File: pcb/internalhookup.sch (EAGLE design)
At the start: 8 parts, among them CN1 LASER, J2 SERVO, J5 CONTROL, Q1 600mA/40V, U1 AMS1117-3.3

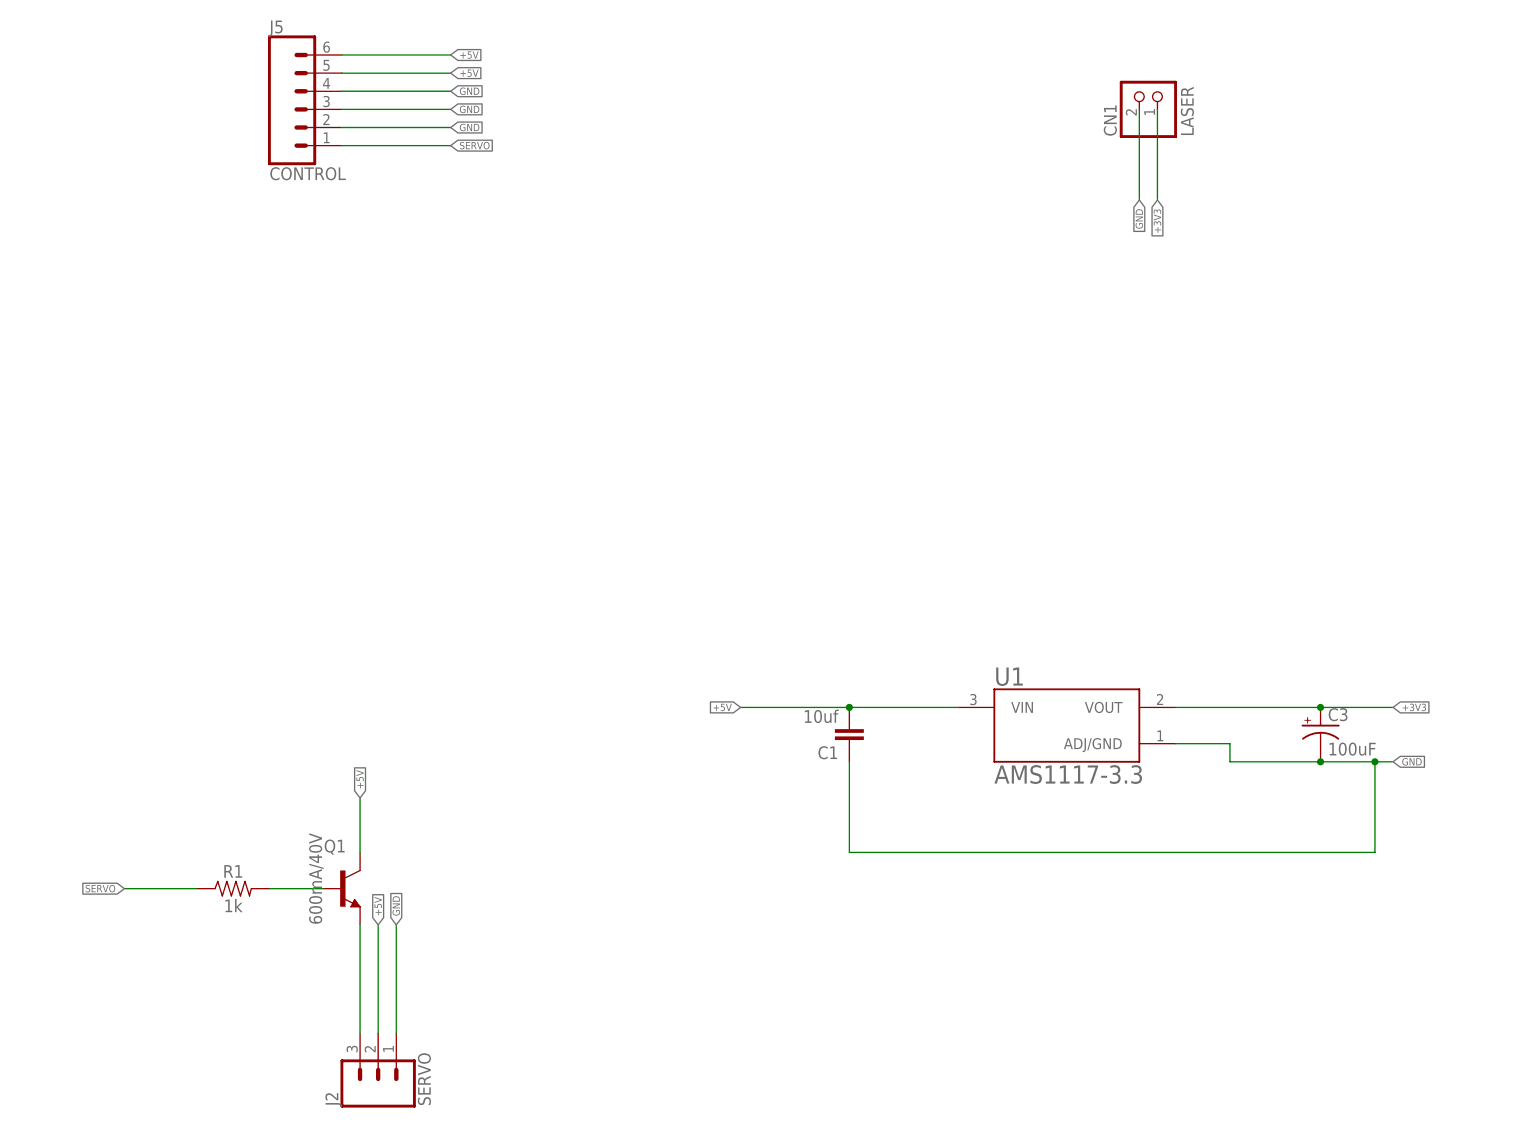
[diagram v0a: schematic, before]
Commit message: Updating to the latest PCB to fix breaking issues
* Fixed capacitor sets for both boards to be larger and polarized on the
LDO's
* Fixed left track for motor board as it was 1 pin too short
* Switched from Declination to Azimuth
* Moved Azimuth signaling to the internal board to allow for movement
* Removed resistors on 5V LED signal buffer
* Switch LED pinout to match the Lumenati ordering
* Internal board got a polarized capacitor
* Internal board layout moved around to better match reality
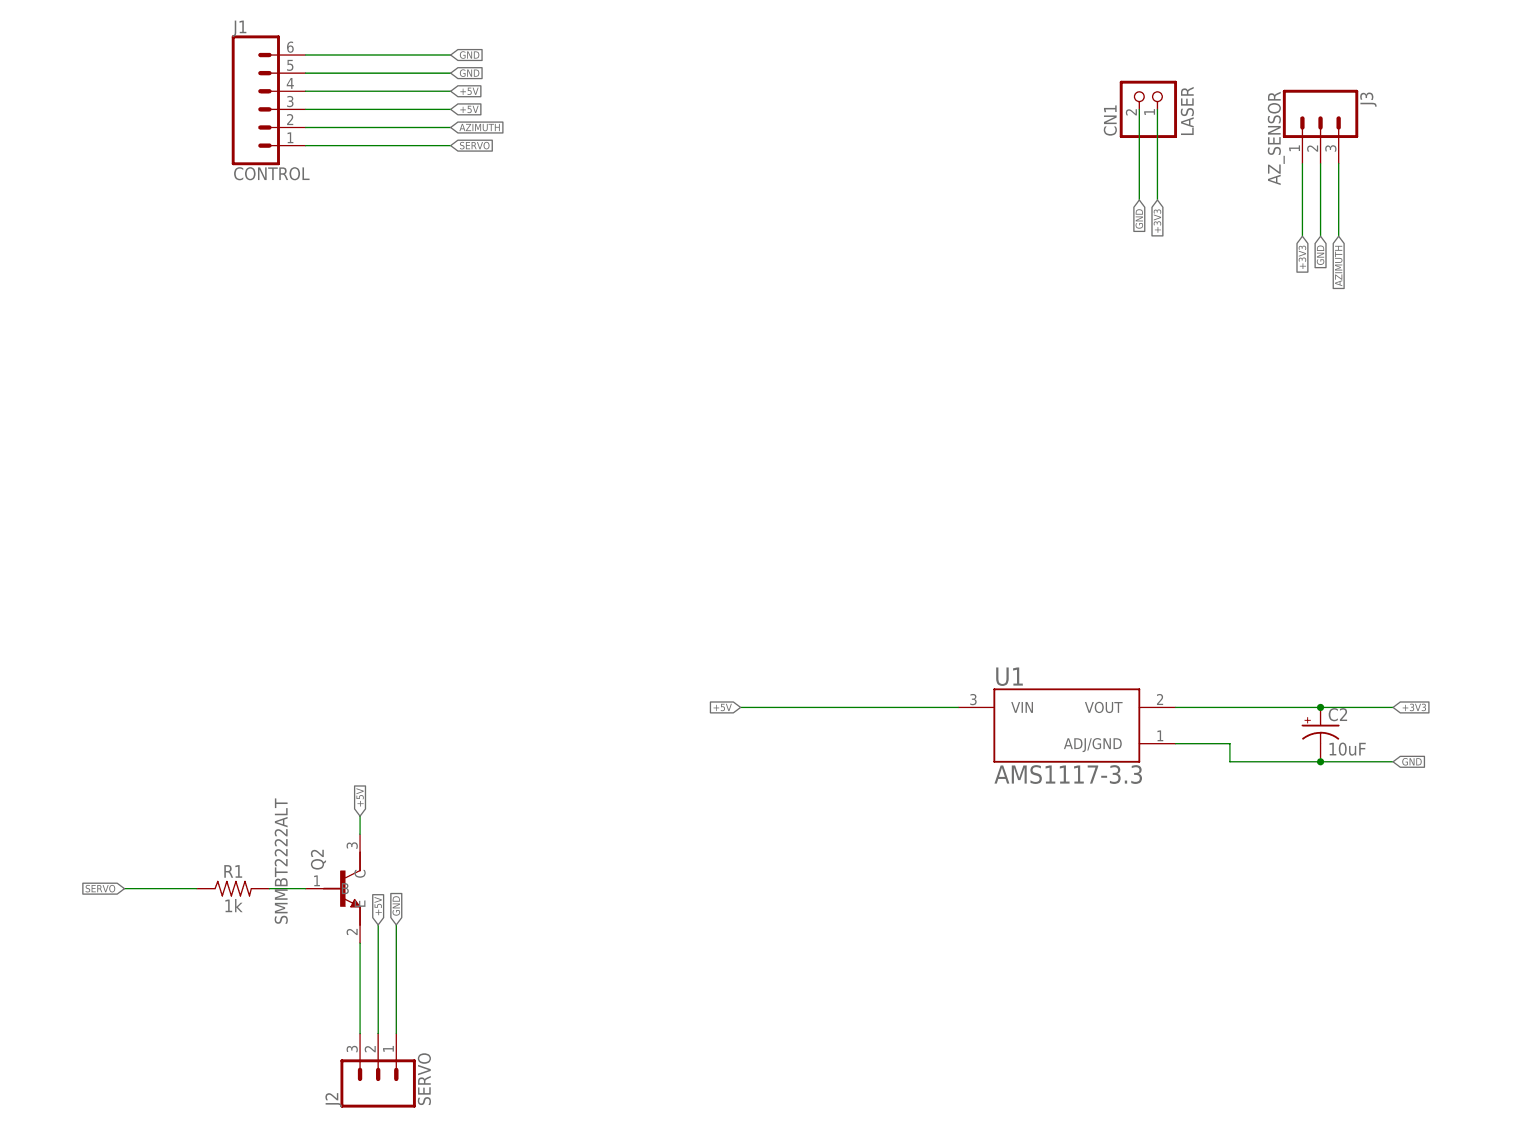
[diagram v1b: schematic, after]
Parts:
- removed C1: 10uf, SparkFun-Capacitors:1.0UF-0805-25V-10%
- removed C3: 100uF, SparkFun-Capacitors:100UF-POLAR-RADIAL-2.5MM-25V-20%
- removed J5: CONTROL, SparkFun-Connectors:CONN_06SILK_FEMALE_PTH
- removed Q1: 600mA/40V, SparkFun-DiscreteSemi:TRANS_NPN-MMBT2222AL
- added C2: 10uF, SparkFun-Capacitors:10UF-POLAR-RADIAL-2.5MM-25V-20%
- added J1: CONTROL, SparkFun-Connectors:CONN_06SILK_FEMALE_PTH
- added J3: AZ_SENSOR, SparkFun-Connectors:CONN_03
- added Q2: SMMBT2222ALT, MMBT3904:MMBT3904
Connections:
- new net AZIMUTH: J1.2, J3.3
- net +3V3: now also C2.+, J3.1; no longer C3.+
- net +5V: now also J1.3, J1.4, Q2.C; no longer C1.2, J5.5, J5.6, Q1.C
- net GND: now also C2.-, J1.5, J1.6, J3.2; no longer C1.1, C3.-, J5.2, J5.3, J5.4
- net N$1: now also Q2.B; no longer Q1.B
- net N$2: now also Q2.E; no longer Q1.E
- net SERVO: now also J1.1; no longer J5.1

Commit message: Adding laser control
* Hookup an NPN to be able to turn the laser on/off via A0
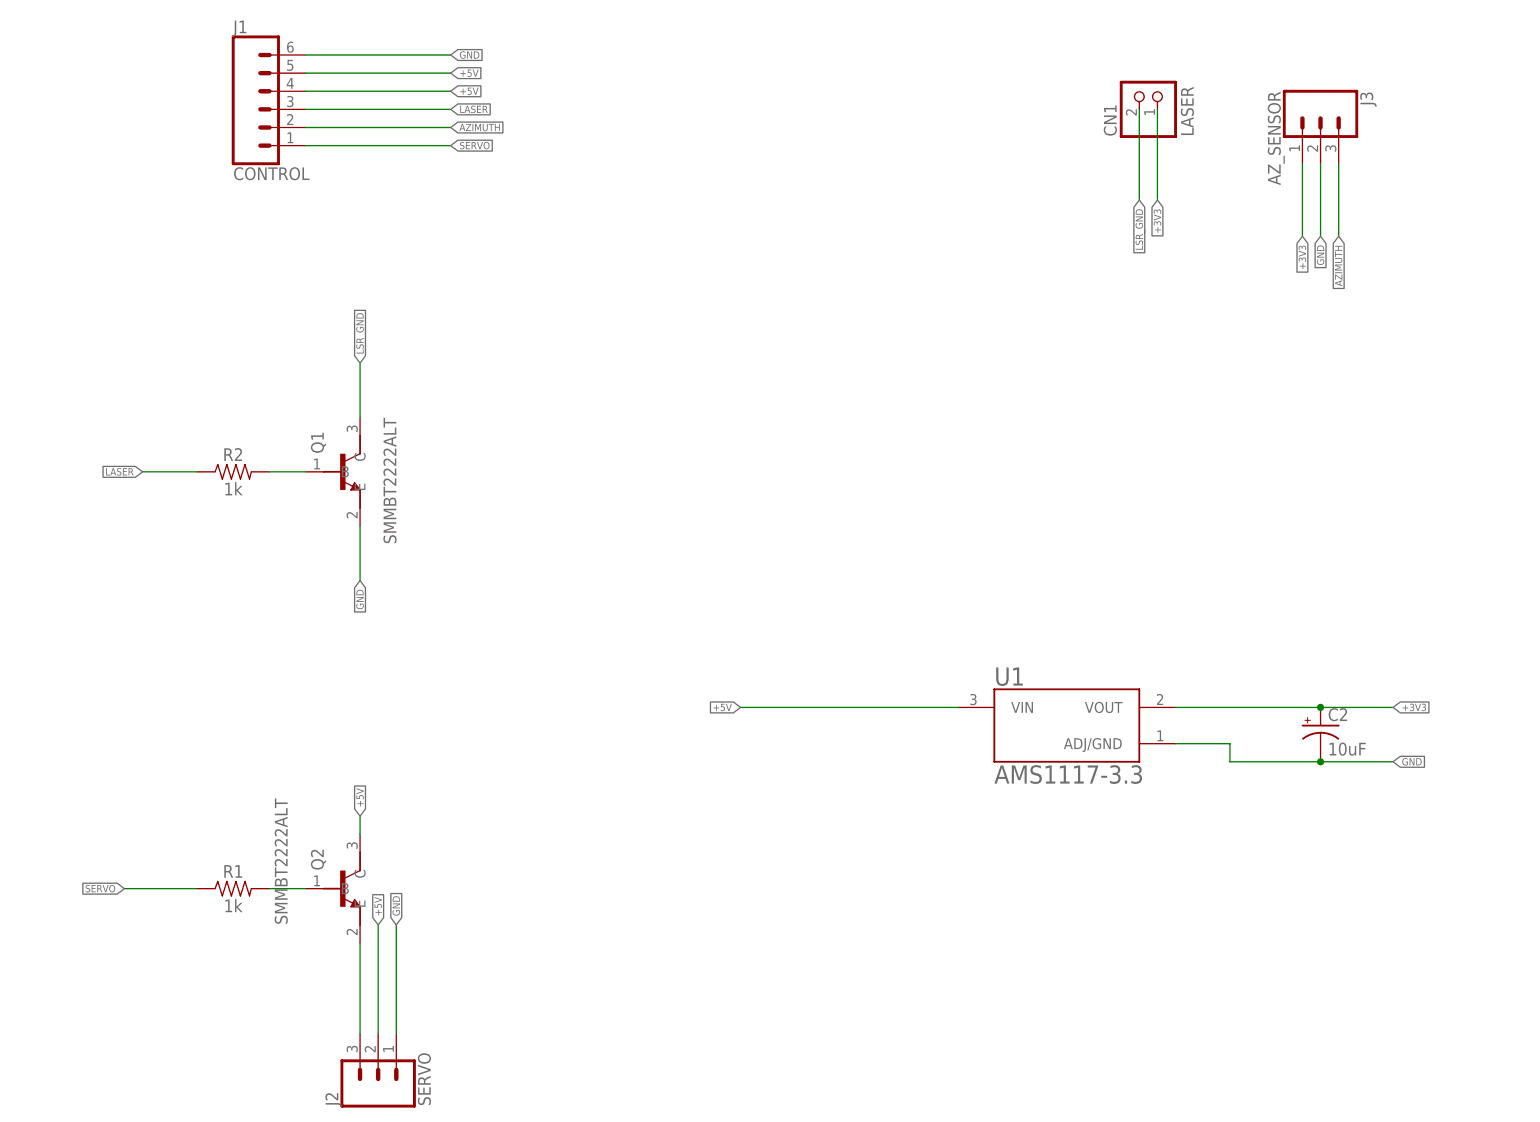
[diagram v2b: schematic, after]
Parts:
- added Q1: SMMBT2222ALT, MMBT3904:MMBT3904
- added R2: 1k, SparkFun-Resistors:0.3OHM-0805-1/8W-1%
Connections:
- new net LASER: J1.3, R2.1
- new net LSR_GND: CN1.1, Q1.C
- new net N$3: Q1.B, R2.2
- net +5V: now also J1.5; no longer J1.3
- net GND: now also Q1.E; no longer CN1.1, J1.5
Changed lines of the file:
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@@
 <part name="J3" library="SparkFun-Connectors" library_urn="urn:adsk.eagle:library:513" deviceset="CONN_03" device="" package3d_urn="urn:adsk.eagle:package:38063/1" value="AZ_SENSOR"/>
 <part name="Q2" library="MMBT3904" deviceset="MMBT3904" device="" value="SMMBT2222ALT"/>
+<part name="Q1" library="MMBT3904" deviceset="MMBT3904" device="" value="SMMBT2222ALT"/>
+<part name="R2" library="SparkFun-Resistors" library_urn="urn:adsk.eagle:library:532" deviceset="0.3OHM" device="-0805-1/8W-1%" package3d_urn="urn:adsk.eagle:package:39651/1" value="1k"/>
 </parts>
 <sheets>
@@
 <attribute name="VALUE" x="53.34501875" y="66.050040625" size="1.781509375" layer="96" rot="R90"/>
 </instance>
+<instance part="Q1" gate="G$1" x="60.96" y="129.54" smashed="yes">
+<attribute name="NAME" x="58.42" y="132.083840625" size="1.779340625" layer="95" rot="R90"/>
+<attribute name="VALUE" x="68.58501875" y="119.390040625" size="1.781509375" layer="96" rot="R90"/>
+</instance>
+<instance part="R2" gate="G$1" x="45.72" y="129.54" smashed="yes">
+<attribute name="NAME" x="45.72" y="131.064" size="1.778" layer="95" font="vector" align="bottom-center"/>
+<attribute name="VALUE" x="45.72" y="128.016" size="1.778" layer="96" font="vector" align="top-center"/>
+</instance>
 </instances>
 <busses>
@@
 </segment>
 <segment>
-<wire x1="172.72" y1="180.34" x2="172.72" y2="167.64" width="0.1524" layer="91"/>
-<label x="172.72" y="167.64" size="1.016" layer="95" rot="R270" xref="yes"/>
-<pinref part="CN1" gate="G$1" pin="1"/>
+<wire x1="55.88" y1="187.96" x2="76.2" y2="187.96" width="0.1524" layer="91"/>
+<label x="76.2" y="187.96" size="1.016" layer="95" xref="yes"/>
+<pinref part="J1" gate="G$1" pin="6"/>
+</segment>
+<segment>
+<pinref part="J3" gate="J$1" pin="2"/>
+<wire x1="198.12" y1="172.72" x2="198.12" y2="162.56" width="0.1524" layer="91"/>
+<label x="198.12" y="162.56" size="1.016" layer="95" rot="R270" xref="yes"/>
+</segment>
+<segment>
+<pinref part="Q1" gate="G$1" pin="E"/>
+<wire x1="63.5" y1="121.92" x2="63.5" y2="114.3" width="0.1524" layer="91"/>
+<label x="63.5" y="114.3" size="1.016" layer="95" rot="R270" xref="yes"/>
+</segment>
+</net>
+<net name="+5V" class="0">
+<segment>
+<label x="116.84" y="96.52" size="1.016" layer="95" rot="R180" xref="yes"/>
+<wire x1="116.84" y1="96.52" x2="147.32" y2="96.52" width="0.1524" layer="91"/>
+<pinref part="U1" gate="G$1" pin="VIN"/>
+</segment>
+<segment>
+<wire x1="63.5" y1="78.74" x2="63.5" y2="81.28" width="0.1524" layer="91"/>
+<label x="63.5" y="81.28" size="1.016" layer="95" rot="R90" xref="yes"/>
+<pinref part="Q2" gate="G$1" pin="C"/>
+</segment>
+<segment>
+<pinref part="J2" gate="J$1" pin="2"/>
+<wire x1="66.04" y1="50.8" x2="66.04" y2="66.04" width="0.1524" layer="91"/>
+<label x="66.04" y="66.04" size="1.016" layer="95" rot="R90" xref="yes"/>
+</segment>
+<segment>
+<wire x1="55.88" y1="182.88" x2="76.2" y2="182.88" width="0.1524" layer="91"/>
+<label x="76.2" y="182.88" size="1.016" layer="95" xref="yes"/>
+<pinref part="J1" gate="G$1" pin="4"/>
 </segment>
 <segment>
@@
 <label x="76.2" y="185.42" size="1.016" layer="95" xref="yes"/>
 <pinref part="J1" gate="G$1" pin="5"/>
-</segment>
-<segment>
-<wire x1="55.88" y1="187.96" x2="76.2" y2="187.96" width="0.1524" layer="91"/>
-<label x="76.2" y="187.96" size="1.016" layer="95" xref="yes"/>
-<pinref part="J1" gate="G$1" pin="6"/>
-</segment>
-<segment>
-<pinref part="J3" gate="J$1" pin="2"/>
-<wire x1="198.12" y1="172.72" x2="198.12" y2="162.56" width="0.1524" layer="91"/>
-<label x="198.12" y="162.56" size="1.016" layer="95" rot="R270" xref="yes"/>
-</segment>
-</net>
-<net name="+5V" class="0">
-<segment>
-<label x="116.84" y="96.52" size="1.016" layer="95" rot="R180" xref="yes"/>
-<wire x1="116.84" y1="96.52" x2="147.32" y2="96.52" width="0.1524" layer="91"/>
-<pinref part="U1" gate="G$1" pin="VIN"/>
-</segment>
-<segment>
-<wire x1="63.5" y1="78.74" x2="63.5" y2="81.28" width="0.1524" layer="91"/>
-<label x="63.5" y="81.28" size="1.016" layer="95" rot="R90" xref="yes"/>
-<pinref part="Q2" gate="G$1" pin="C"/>
-</segment>
-<segment>
-<pinref part="J2" gate="J$1" pin="2"/>
-<wire x1="66.04" y1="50.8" x2="66.04" y2="66.04" width="0.1524" layer="91"/>
-<label x="66.04" y="66.04" size="1.016" layer="95" rot="R90" xref="yes"/>
-</segment>
-<segment>
-<wire x1="55.88" y1="180.34" x2="76.2" y2="180.34" width="0.1524" layer="91"/>
-<label x="76.2" y="180.34" size="1.016" layer="95" xref="yes"/>
-<pinref part="J1" gate="G$1" pin="3"/>
-</segment>
-<segment>
-<wire x1="55.88" y1="182.88" x2="76.2" y2="182.88" width="0.1524" layer="91"/>
-<label x="76.2" y="182.88" size="1.016" layer="95" xref="yes"/>
-<pinref part="J1" gate="G$1" pin="4"/>
 </segment>
 </net>
@@
 </segment>
 </net>
+<net name="LASER" class="0">
+<segment>
+<wire x1="55.88" y1="180.34" x2="76.2" y2="180.34" width="0.1524" layer="91"/>
+<label x="76.2" y="180.34" size="1.016" layer="95" xref="yes"/>
+<pinref part="J1" gate="G$1" pin="3"/>
+</segment>
+<segment>
+<pinref part="R2" gate="G$1" pin="1"/>
+<wire x1="40.64" y1="129.54" x2="33.02" y2="129.54" width="0.1524" layer="91"/>
+<label x="33.02" y="129.54" size="1.016" layer="95" rot="R180" xref="yes"/>
+</segment>
+</net>
+<net name="N$3" class="0">
+<segment>
+<pinref part="Q1" gate="G$1" pin="B"/>
+<pinref part="R2" gate="G$1" pin="2"/>
+<wire x1="55.88" y1="129.54" x2="50.8" y2="129.54" width="0.1524" layer="91"/>
+</segment>
+</net>
+<net name="LSR_GND" class="0">
+<segment>
+<pinref part="Q1" gate="G$1" pin="C"/>
+<wire x1="63.5" y1="137.16" x2="63.5" y2="144.78" width="0.1524" layer="91"/>
+<label x="63.5" y="144.78" size="1.016" layer="95" rot="R90" xref="yes"/>
+</segment>
+<segment>
+<wire x1="172.72" y1="180.34" x2="172.72" y2="167.64" width="0.1524" layer="91"/>
+<label x="172.72" y="167.64" size="1.016" layer="95" rot="R270" xref="yes"/>
+<pinref part="CN1" gate="G$1" pin="1"/>
+</segment>
+</net>
